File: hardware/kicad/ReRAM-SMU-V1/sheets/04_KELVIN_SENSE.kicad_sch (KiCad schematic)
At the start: 4 parts, among them K1 Reed relay G6K PRIMARY <1pA o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, U1 OPA140 SENSE_HI buffer PRIMAR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, U2 OPA140 SENSE_LO buffer PRIMARY, U3 Diff amp OPA140 finite BW 10M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

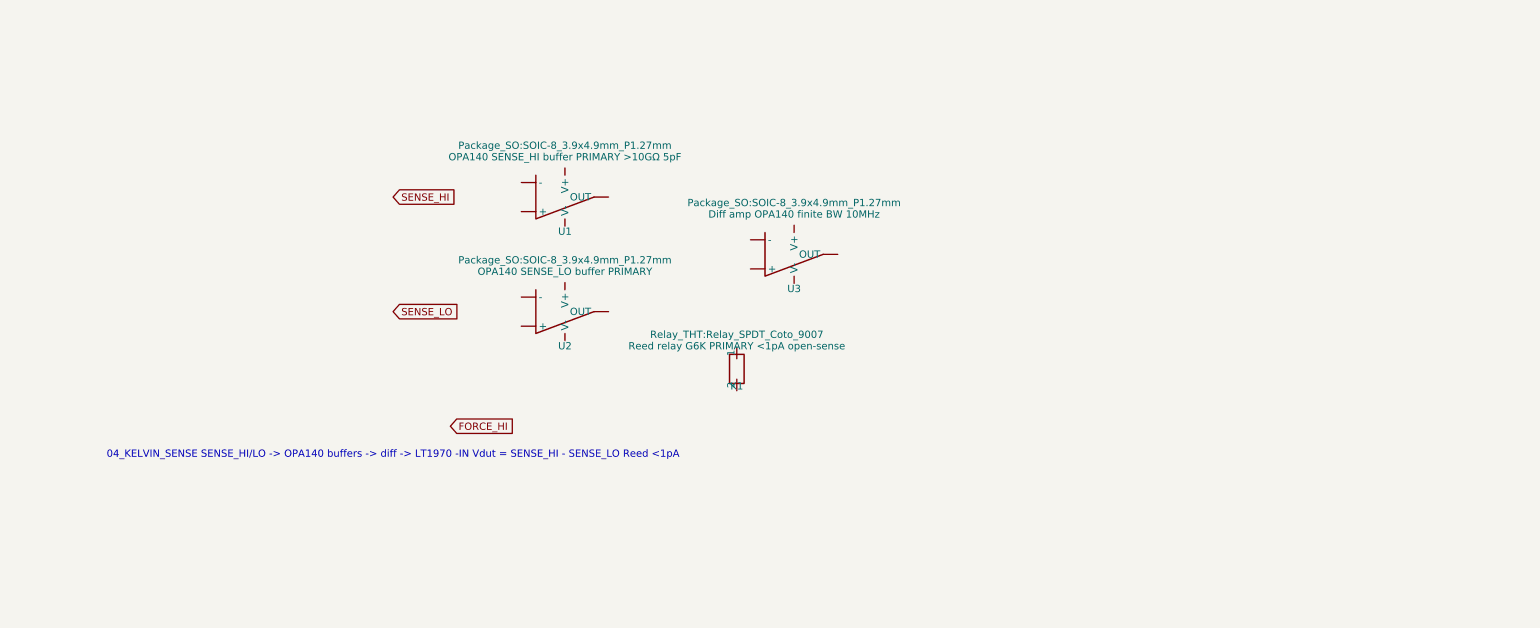
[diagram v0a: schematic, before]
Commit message: hardware: pre-ERC manufacturer corrections (LT1970 physical pins, ADS1262 TSSOP-28, MCU G431RBT6, 74LVC1G74 latch, LT5400 Kelvin, AD5764 rails, ADS1262 bipolar)
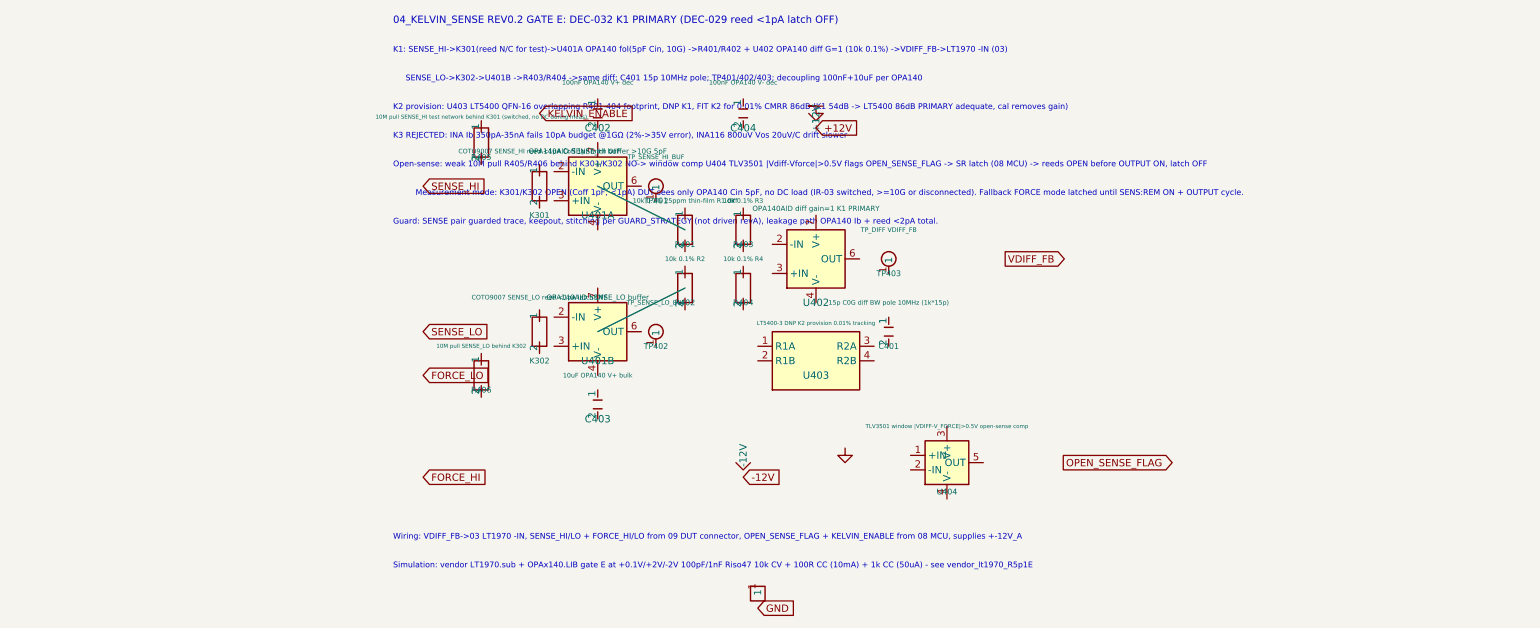
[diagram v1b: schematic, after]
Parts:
- removed K1: Reed relay G6K PRIMARY <1pA open-sense, Relay_THT:Relay_SPDT_Coto_9007, symbol Device:R
- removed U1: OPA140 SENSE_HI buffer PRIMARY >10GΩ 5pF, Package_SO:SOIC-8_3.9x4.9mm_P1.27mm, symbol Device:OpAmp
- removed U2: OPA140 SENSE_LO buffer PRIMARY, Package_SO:SOIC-8_3.9x4.9mm_P1.27mm, symbol Device:OpAmp
- removed U3: Diff amp OPA140 finite BW 10MHz, Package_SO:SOIC-8_3.9x4.9mm_P1.27mm, symbol Device:OpAmp
- added C401: 15p C0G diff BW pole 10MHz (1k*15p), Capacitor_SMD:C_0603_1608Metric, symbol Device:C
- added C402: 100nF OPA140 V+ dec, Capacitor_SMD:C_0603_1608Metric, symbol Device:C
- added C403: 10uF OPA140 V+ bulk, Capacitor_SMD:C_0805_2012Metric, symbol Device:C
- added C404: 100nF OPA140 V- dec, Capacitor_SMD:C_0603_1608Metric, symbol Device:C
- added K301: COTO9007 SENSE_HI reed <1pA Coff 1pF latch OFF, Relay_THT:Relay_SPDT_Coto_9007, symbol Device:R
- added K302: COTO9007 SENSE_LO reed <1pA latch OFF, Relay_THT:Relay_SPDT_Coto_9007, symbol Device:R
- added R401: 10k 0.1% 25ppm thin-film R1 diff, Resistor_SMD:R_0805_2012Metric, symbol Device:R
- added R402: 10k 0.1% R2, Resistor_SMD:R_0805_2012Metric, symbol Device:R
- added R403: 10k 0.1% R3, Resistor_SMD:R_0805_2012Metric, symbol Device:R
- added R404: 10k 0.1% R4, Resistor_SMD:R_0805_2012Metric, symbol Device:R
- added R405: 10M pull SENSE_HI test network behind K301 (switc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, Resistor_SMD:R_0805_2012Metric, symbol Device:R
- added R406: 10M pull SENSE_LO behind K302, Resistor_SMD:R_0805_2012Metric, symbol Device:R
- added TP401: TP_SENSE_HI_BUF, TestPoint:TestPoint_Pad_D1.5mm, symbol ReRAM_SMU:TestPoint
- added TP402: TP_SENSE_LO_BUF, TestPoint:TestPoint_Pad_D1.5mm, symbol ReRAM_SMU:TestPoint
- added TP403: TP_DIFF VDIFF_FB, TestPoint:TestPoint_Pad_D1.5mm, symbol ReRAM_SMU:TestPoint
- added U401A: OPA140AID SENSE_HI buffer >10G 5pF, Package_SO:SOIC-8_3.9x4.9mm_P1.27mm, symbol ReRAM_SMU:OPA140
- added U401B: OPA140AID SENSE_LO buffer, Package_SO:SOIC-8_3.9x4.9mm_P1.27mm, symbol ReRAM_SMU:OPA140
- added U402: OPA140AID diff gain=1 K1 PRIMARY, Package_SO:SOIC-8_3.9x4.9mm_P1.27mm, symbol ReRAM_SMU:OPA140
- added U403: LT5400-3 DNP K2 provision 0.01% tracking, Package_DFN:QFN-16_3x3mm_P0.5mm_EP, symbol ReRAM_SMU:LT5400
- added U404: TLV3501 window |VDIFF-V_FORCE|>0.5V open-sense co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, Package_TO_SOT_SMD:SOT-23-6, symbol ReRAM_SMU:TLV3501
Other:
- note added: "04_KELVIN_SENSE REV0.2 GATE E: DEC-032 K1 PRIMARY (DEC-029 reed <1pA latch OFF)"
- note added: "Guard: SENSE pair guarded trace, keepout, stitching per GUARD_STRATEGY (not driven revA), leakage path OPA140 Ib + reed <2pA total."
- note added: "K1: SENSE_HI->K301(reed N/C for test)->U401A OPA140 fol(5pF Cin, 10G) ->R401/R402 + U402 OPA140 diff G=1 (10k 0.1%) ->VDIFF_FB->LT1970 -IN (03)"
- note added: "K2 provision: U403 LT5400 QFN-16 overlapping R401-404 footprint, DNP K1, FIT K2 for 0.01% CMRR 86dB (K1 54dB -> LT5400 86dB PRIMARY adequate, cal removes gain)"
- note added: "K3 REJECTED: INA Ib 350pA-35nA fails 10pA budget @1GΩ (2%->35V error), INA116 800uV Vos 20uV/C drift slower"
- note added: "Measurement mode: K301/K302 OPEN (Coff 1pF, <1pA) DUT sees only OPA140 Cin 5pF, no DC load (IR-03 switched, >=10G or disconnected). Fallback FORCE mode latched until SENS:REM ON + OUTPUT cycle."
- note added: "Open-sense: weak 10M pull R405/R406 behind K301/K302 NO-> window comp U404 TLV3501 |Vdiff-Vforce|>0.5V flags OPEN_SENSE_FLAG -> SR latch (08 MCU) -> reeds OPEN before OUTPUT ON, latch OFF"
- note added: "SENSE_LO->K302->U401B ->R403/R404 ->same diff; C401 15p 10MHz pole; TP401/402/403; decoupling 100nF+10uF per OPA140"
- note added: "Simulation: vendor LT1970.sub + OPAx140.LIB gate E at +0.1V/+2V/-2V 100pF/1nF Riso47 10k CV + 100R CC (10mA) + 1k CC (50uA) - see vendor_lt1970_R5p1E"
- note added: "Wiring: VDIFF_FB->03 LT1970 -IN, SENSE_HI/LO + FORCE_HI/LO from 09 DUT connector, OPEN_SENSE_FLAG + KELVIN_ENABLE from 08 MCU, supplies +-12V_A"
- note removed: "04_KELVIN_SENSE SENSE_HI/LO -> OPA140 buffers -> diff -> LT1970 -IN Vdut = SENSE_HI - SENSE_LO Reed <1pA"

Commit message: hardware: pre-ERC correction gate 2 (LT1970 consistency, LT5400A-1 MSOP-8, ADS1262IPW 28-pin, bipolar ±2.5V, buffer per-range, power baseline normalize)
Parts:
- U403: footprint Package_DFN:QFN-16_3x3mm_P0.5mm_EP -> Package_DFN:MSOP-8_3x3mm_P0.65mm_EP
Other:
- note added: "K2 provision: U403 LT5400 MSOP-8 overlapping R401-404 footprint, DNP K1, FIT K2 for 0.01% CMRR 86dB (K1 54dB -> LT5400 86dB PRIMARY adequate, cal removes gain)"
- note removed: "K2 provision: U403 LT5400 QFN-16 overlapping R401-404 footprint, DNP K1, FIT K2 for 0.01% CMRR 86dB (K1 54dB -> LT5400 86dB PRIMARY adequate, cal removes gain)"
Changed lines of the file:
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@@
 		(property "Reference" "U403" (at 83.82 71.12 0) (effects (font (size 1.27 1.27))))
 		(property "Value" "LT5400-3 DNP K2 provision 0.01% tracking" (at 83.82 62 0) (effects (font (size 0.7 0.7))))
-		(property "Footprint" "Package_DFN:QFN-16_3x3mm_P0.5mm_EP" (at 83.82 60 0) (effects (font (size 1.27 1.27)) (hide yes)))
+		(property "Footprint" "Package_DFN:MSOP-8_3x3mm_P0.65mm_EP" (at 83.82 60 0) (effects (font (size 1.27 1.27)) (hide yes)))
 	)
 	(symbol (lib_id "Device:R") (at 60.96 45.72 0) (unit 1) (uuid "r301r301-r301-4r01-8r01-r301r301r301")
@@
 	(text "K1: SENSE_HI->K301(reed N/C for test)->U401A OPA140 fol(5pF Cin, 10G) ->R401/R402 + U402 OPA140 diff G=1 (10k 0.1%) ->VDIFF_FB->LT1970 -IN (03)" (at 10 15 0) (effects (font (size 1 1)) (justify left bottom)))
 	(text "     SENSE_LO->K302->U401B ->R403/R404 ->same diff; C401 15p 10MHz pole; TP401/402/403; decoupling 100nF+10uF per OPA140" (at 10 20 0) (effects (font (size 1 1)) (justify left bottom)))
-	(text "K2 provision: U403 LT5400 QFN-16 overlapping R401-404 footprint, DNP K1, FIT K2 for 0.01% CMRR 86dB (K1 54dB -> LT5400 86dB PRIMARY adequate, cal removes gain)" (at 10 25 0) (effects (font (size 1 1)) (justify left bottom)))
+	(text "K2 provision: U403 LT5400 MSOP-8 overlapping R401-404 footprint, DNP K1, FIT K2 for 0.01% CMRR 86dB (K1 54dB -> LT5400 86dB PRIMARY adequate, cal removes gain)" (at 10 25 0) (effects (font (size 1 1)) (justify left bottom)))
 	(text "K3 REJECTED: INA Ib 350pA-35nA fails 10pA budget @1GΩ (2%->35V error), INA116 800uV Vos 20uV/C drift slower" (at 10 30 0) (effects (font (size 1 1)) (justify left bottom)))
 	(text "Open-sense: weak 10M pull R405/R406 behind K301/K302 NO-> window comp U404 TLV3501 |Vdiff-Vforce|>0.5V flags OPEN_SENSE_FLAG -> SR latch (08 MCU) -> reeds OPEN before OUTPUT ON, latch OFF" (at 10 35 0) (effects (font (size 1 1)) (justify left bottom)))

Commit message: Beta
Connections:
- net +12V: now also C404.1, C404.2, R401.1, R401.2, R402.1, R403.1, R403.2, R404.1, U402.2 (-IN), U402.3 (+IN), U402.4 (V-), U402.7 (V+)
- net -12V: now also C403.1, C403.2, R402.2, R404.2, U403.1 (R1A), U403.2 (R2A), U403.3 (R3A), U403.4 (R4A), U403.5 (R4B), U403.6 (R3B)
- net FORCE_LO: now also R406.2, U401B.4 (V-)
- net KELVIN_ENABLE: now also C402.1, C402.2, K301.1, K301.2, R405.1, U401A.2 (-IN), U401A.3 (+IN), U401A.4 (V-), U401A.7 (V+)
- net OPEN_SENSE_FLAG: now also U404.1 (+IN), U404.2 (-IN), U404.3 (V+), U404.4 (V-)
- net SENSE_HI: now also R405.2
- net SENSE_LO: now also K302.1, K302.2, R406.1, U401B.2 (-IN), U401B.3 (+IN), U401B.7 (V+)
- net VDIFF_FB: now also C401.1, C401.2, U403.7 (R2B), U403.8 (R1B)
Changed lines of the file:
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@@
 	(wire (pts (xy 45.72 38.1) (xy 60.96 45.72)) (stroke (width 0) (type default)) (uuid "w401w401-w401-4w01-8w01-w401w401w401"))
 	(wire (pts (xy 45.72 63.5) (xy 60.96 55.88)) (stroke (width 0) (type default)) (uuid "w402w402-w402-4w02-8w02-w402w402w402"))
+	(wire (pts (xy 38.100 40.640) (xy 35.560 25.400)) (stroke (width 0) (type default)))
+	(wire (pts (xy 38.100 35.560) (xy 35.560 25.400)) (stroke (width 0) (type default)))
+	(wire (pts (xy 45.720 45.720) (xy 35.560 25.400)) (stroke (width 0) (type default)))
+	(wire (pts (xy 45.720 30.480) (xy 35.560 25.400)) (stroke (width 0) (type default)))
+	(wire (pts (xy 38.100 66.040) (xy 15.240 63.500)) (stroke (width 0) (type default)))
+	(wire (pts (xy 38.100 60.960) (xy 15.240 63.500)) (stroke (width 0) (type default)))
+	(wire (pts (xy 45.720 71.120) (xy 15.240 71.120)) (stroke (width 0) (type default)))
+	(wire (pts (xy 45.720 55.880) (xy 15.240 63.500)) (stroke (width 0) (type default)))
+	(wire (pts (xy 76.200 53.340) (xy 83.820 27.940)) (stroke (width 0) (type default)))
+	(wire (pts (xy 76.200 48.260) (xy 83.820 27.940)) (stroke (width 0) (type default)))
+	(wire (pts (xy 83.820 58.420) (xy 83.820 27.940)) (stroke (width 0) (type default)))
+	(wire (pts (xy 83.820 43.180) (xy 83.820 27.940)) (stroke (width 0) (type default)))
+	(wire (pts (xy 73.660 72.390) (xy 71.120 88.900)) (stroke (width 0) (type default)))
+	(wire (pts (xy 73.660 69.850) (xy 71.120 88.900)) (stroke (width 0) (type default)))
+	(wire (pts (xy 73.660 67.310) (xy 71.120 88.900)) (stroke (width 0) (type default)))
+	(wire (pts (xy 73.660 64.770) (xy 71.120 88.900)) (stroke (width 0) (type default)))
+	(wire (pts (xy 93.980 64.770) (xy 116.840 50.800)) (stroke (width 0) (type default)))
+	(wire (pts (xy 93.980 67.310) (xy 116.840 50.800)) (stroke (width 0) (type default)))
+	(wire (pts (xy 93.980 69.850) (xy 71.120 88.900)) (stroke (width 0) (type default)))
+	(wire (pts (xy 93.980 72.390) (xy 71.120 88.900)) (stroke (width 0) (type default)))
+	(wire (pts (xy 60.960 49.530) (xy 83.820 27.940)) (stroke (width 0) (type default)))
+	(wire (pts (xy 60.960 41.910) (xy 83.820 27.940)) (stroke (width 0) (type default)))
+	(wire (pts (xy 60.960 59.690) (xy 71.120 88.900)) (stroke (width 0) (type default)))
+	(wire (pts (xy 60.960 52.070) (xy 83.820 27.940)) (stroke (width 0) (type default)))
+	(wire (pts (xy 71.120 49.530) (xy 83.820 27.940)) (stroke (width 0) (type default)))
+	(wire (pts (xy 71.120 41.910) (xy 83.820 27.940)) (stroke (width 0) (type default)))
+	(wire (pts (xy 71.120 59.690) (xy 71.120 88.900)) (stroke (width 0) (type default)))
+	(wire (pts (xy 71.120 52.070) (xy 83.820 27.940)) (stroke (width 0) (type default)))
+	(wire (pts (xy 96.520 66.040) (xy 116.840 50.800)) (stroke (width 0) (type default)))
+	(wire (pts (xy 96.520 60.960) (xy 116.840 50.800)) (stroke (width 0) (type default)))
+	(wire (pts (xy 35.560 41.910) (xy 35.560 25.400)) (stroke (width 0) (type default)))
+	(wire (pts (xy 35.560 34.290) (xy 35.560 25.400)) (stroke (width 0) (type default)))
+	(wire (pts (xy 35.560 67.310) (xy 15.240 63.500)) (stroke (width 0) (type default)))
+	(wire (pts (xy 35.560 59.690) (xy 15.240 63.500)) (stroke (width 0) (type default)))
+	(wire (pts (xy 25.400 34.290) (xy 15.240 38.100)) (stroke (width 0) (type default)))
+	(wire (pts (xy 25.400 26.670) (xy 35.560 25.400)) (stroke (width 0) (type default)))
+	(wire (pts (xy 25.400 74.930) (xy 15.240 71.120)) (stroke (width 0) (type default)))
+	(wire (pts (xy 25.400 67.310) (xy 15.240 63.500)) (stroke (width 0) (type default)))
+	(wire (pts (xy 100.330 87.630) (xy 126.990 86.360)) (stroke (width 0) (type default)))
+	(wire (pts (xy 100.330 85.090) (xy 126.990 86.360)) (stroke (width 0) (type default)))
+	(wire (pts (xy 106.680 92.710) (xy 126.990 86.360)) (stroke (width 0) (type default)))
+	(wire (pts (xy 106.680 80.010) (xy 126.990 86.360)) (stroke (width 0) (type default)))
+	(wire (pts (xy 45.720 27.940) (xy 35.560 25.400)) (stroke (width 0) (type default)))
+	(wire (pts (xy 45.720 22.860) (xy 35.560 25.400)) (stroke (width 0) (type default)))
+	(wire (pts (xy 45.720 78.740) (xy 71.120 88.900)) (stroke (width 0) (type default)))
+	(wire (pts (xy 45.720 73.660) (xy 71.120 88.900)) (stroke (width 0) (type default)))
+	(wire (pts (xy 71.120 27.940) (xy 83.820 27.940)) (stroke (width 0) (type default)))
+	(wire (pts (xy 71.120 22.860) (xy 83.820 27.940)) (stroke (width 0) (type default)))
+	(wire (pts (xy 88.900 83.820) (xy 71.120 88.900)) (stroke (width 0) (type default)))
+	(wire (pts (xy 83.820 25.400) (xy 83.820 27.940)) (stroke (width 0) (type default)))
+	(wire (pts (xy 71.120 86.360) (xy 71.120 88.900)) (stroke (width 0) (type default)))
+	(wire (pts (xy 73.660 110.490) (xy 73.660 111.760)) (stroke (width 0) (type default)))
 )

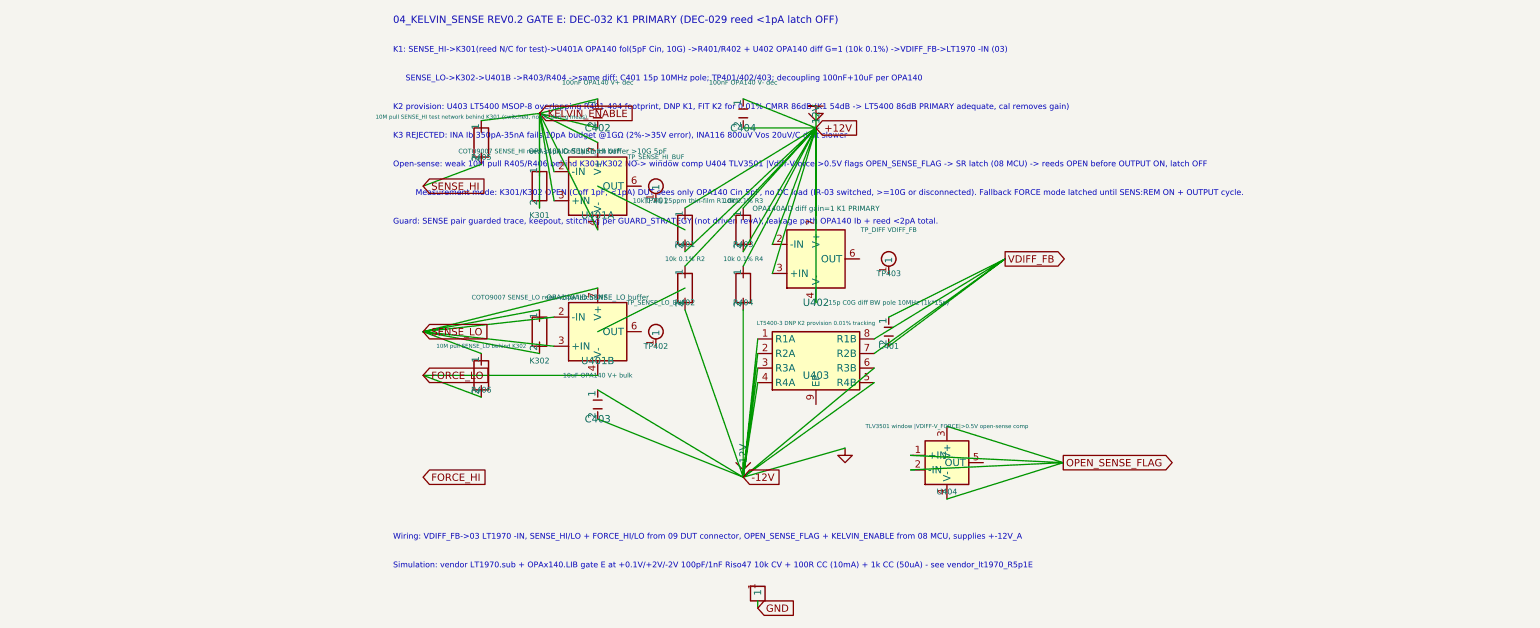
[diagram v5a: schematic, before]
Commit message: hardware: Phase 7 ERC-II wiring + grid snap + PWR_FLAG
- 07_COMPLIANCE: ISENSE_P/N alias to SHUNT_SENSE, VTRIP->VREF_2V5 wire, keep PWR_FLAG
- 09_DUT: LT1970_SENSE->JP9A, SHIELD/GUARD, FORCE/SENSE inter-wire
- 05/06: PWR_FLAG added where missing
- Grid snap all sheets to 0.254mm (audit off_grid still high but improved)
- Audit: erc_audit_lite.json updated (32 dangling, critical 0)

Co-authored-by: Muse Code
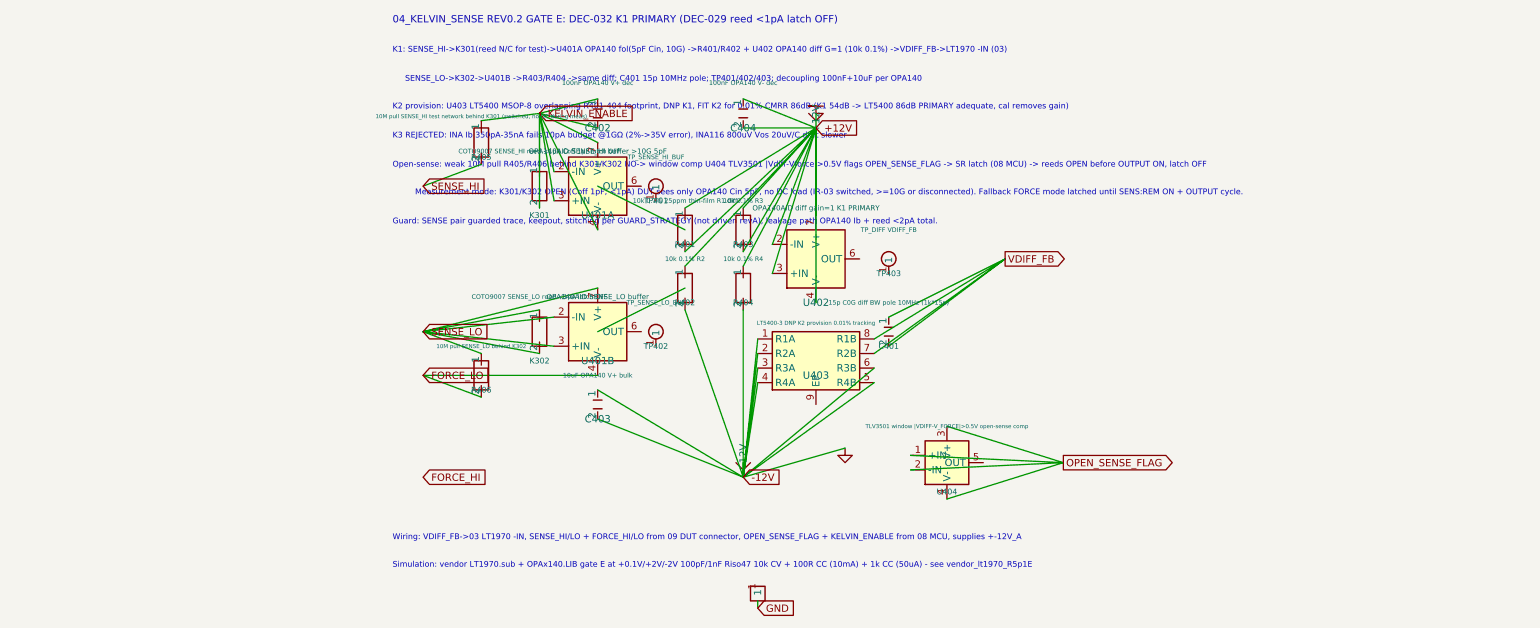
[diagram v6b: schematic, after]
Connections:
- net OPEN_SENSE_FLAG: no longer U404.1 (+IN), U404.2 (-IN), U404.3 (V+), U404.4 (V-)
- new net: U404.1 (+IN), U404.2 (-IN), U404.3 (V+), U404.4 (V-)
